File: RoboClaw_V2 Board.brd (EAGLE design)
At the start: 49 x 23.6 mm, 7 parts

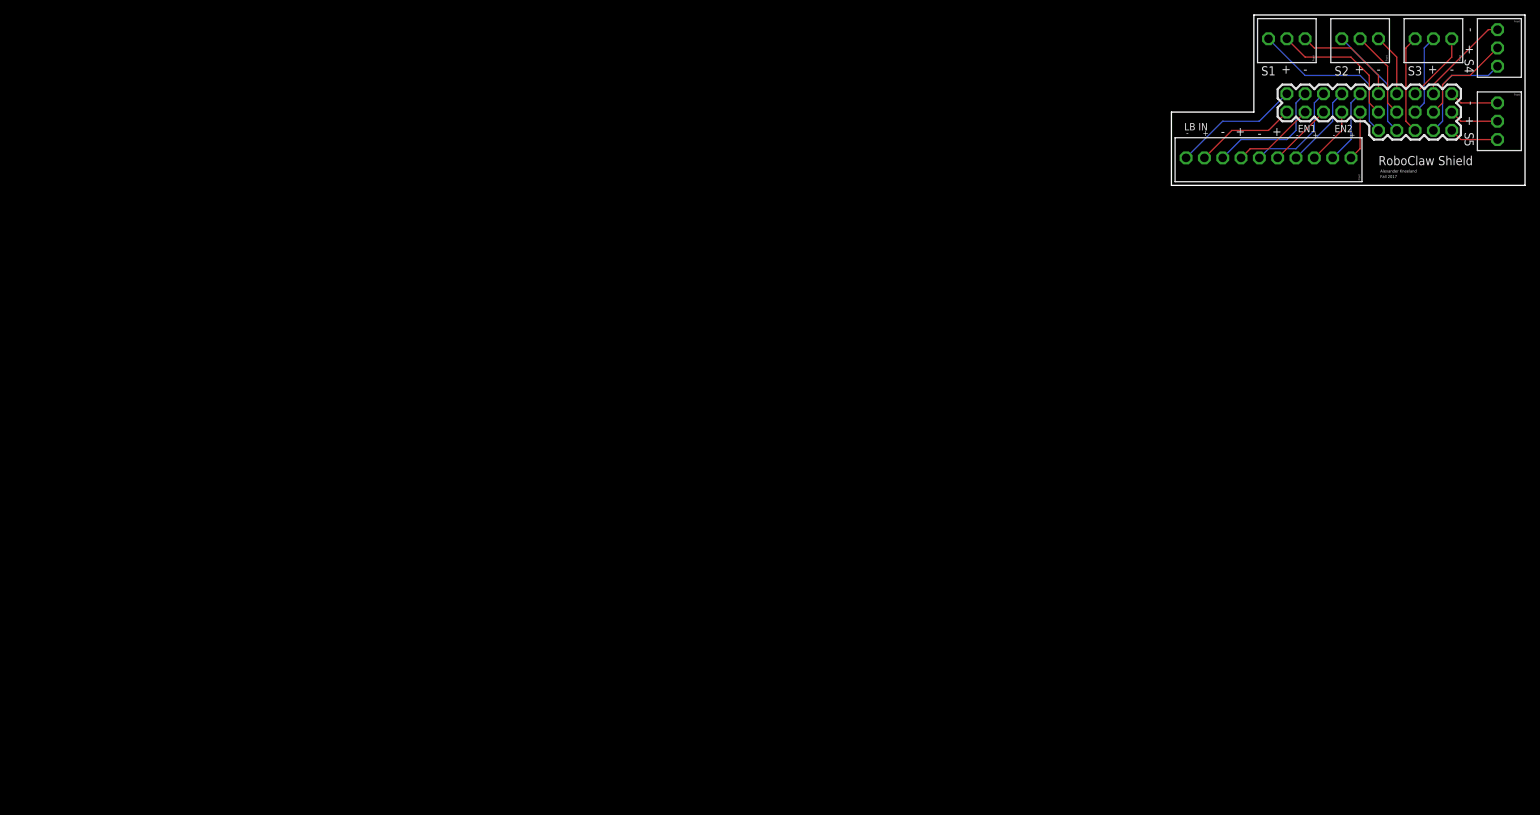
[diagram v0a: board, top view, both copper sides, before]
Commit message: Added in some new connectors in the schematic and resized board
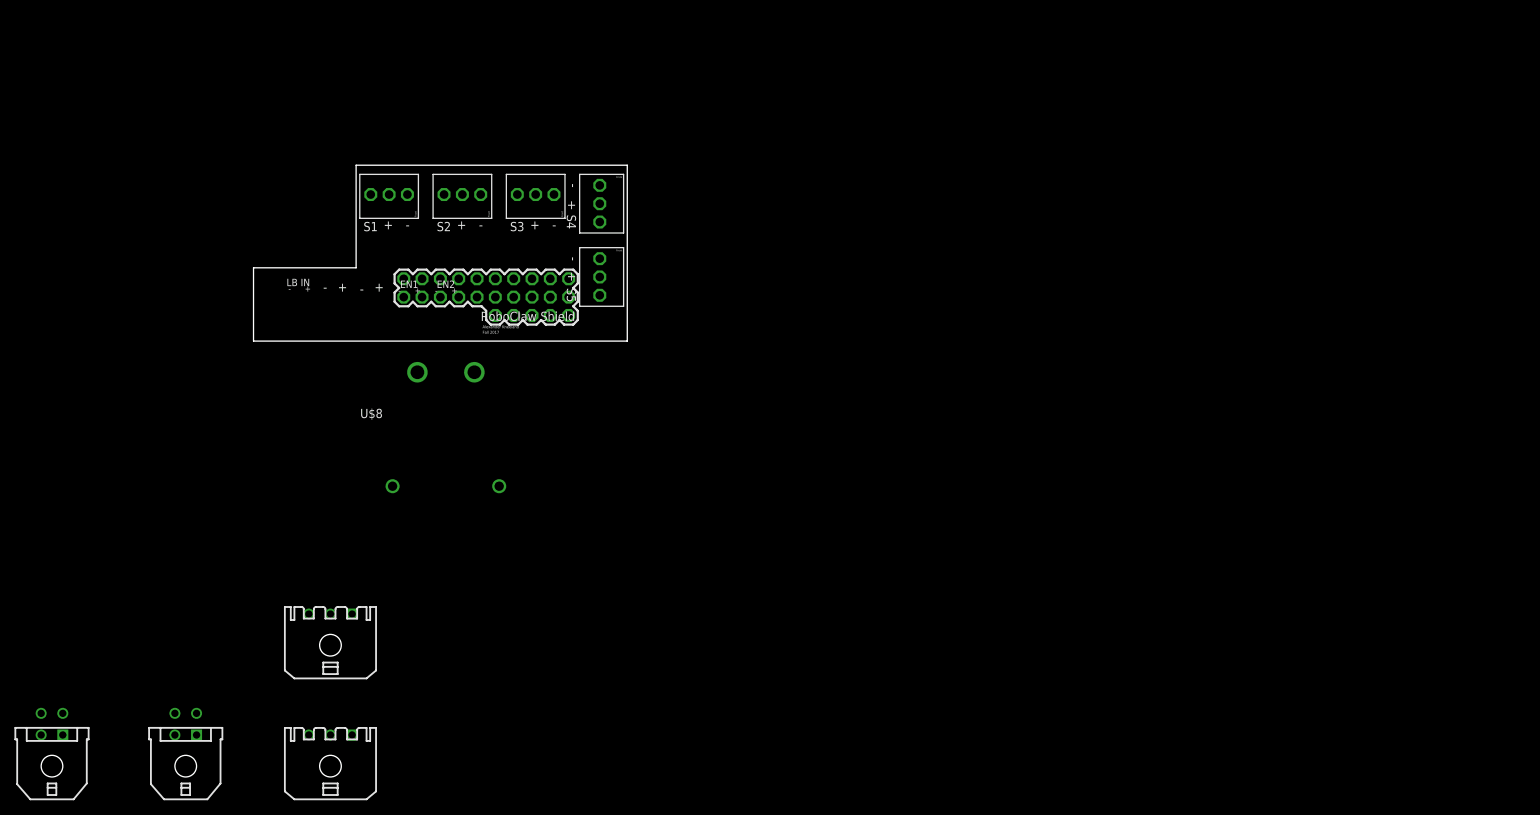
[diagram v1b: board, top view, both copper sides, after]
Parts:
- removed U$2: 10_PIN, Screw Blocks:10_PIN
- added U$8: (no value), 000_CustomPartsMaster:ANDERSON_RIGHTANGLE_X2
- added X1, X2: (no value), con-molex-micro-fit-3_0:43650-0300
- added X3, X4: (no value), con-molex-micro-fit-3_0:43045-0400
- moved U$5 126.3 mm to (-21.6, 21.6)
- moved U$3 126.3 mm to (-5.08, 0.00)
- moved U$4 126.3 mm to (-5.08, 10.2)
- moved U$6 126.3 mm to (-31.8, 21.6)
- moved U$7 126.3 mm to (-41.9, 21.6)
- moved U$1 125.1 mm to (-20.8, 3.56)
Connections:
- removed net N$10: U$1.P$12, U$6.P$1
- removed net N$13: U$1.P$15, U$7.P$1
- removed net N$14: U$1.P$14, U$7.P$2
- removed net N$16: U$1.P$18, U$2.P$3
- removed net N$17: U$1.P$21, U$2.P$6
- removed net N$18: U$1.P$20, U$2.P$5
- removed net N$19: U$1.P$23, U$2.P$8
- removed net N$20: U$1.P$22, U$2.P$7
- removed net N$21: U$1.P$24, U$2.P$9
- removed net N$22: U$1.P$25, U$2.P$10
- removed net N$24: U$1.P$17, U$2.P$2
- removed net N$25: U$1.P$16, U$2.P$1
- removed net N$26: U$1.P$19, U$2.P$4
- removed net N$28: U$1.P$13, U$7.P$3
- removed net N$4: U$1.P$6, U$4.P$1
- removed net N$5: U$1.P$5, U$4.P$2
- new net EN1_+: U$1.P$20
- new net EN1_A: U$1.P$18
- new net EN2_+: U$1.P$22
- new net EN2_A: U$1.P$16
- new net LB_+: U$1.P$24
- new net N$29: U$1.P$12
- new net N$30: U$1.P$11
- new net N$31: U$1.P$10
- new net N$32: U$1.P$15
- new net N$33: U$1.P$14
- net N$1: now also U$1.P$17; no longer U$1.P$1, U$3.P$3
- net N$11: now also U$1.P$5; no longer U$1.P$11, U$6.P$2
- net N$12: now also U$1.P$4; no longer U$1.P$10, U$6.P$3
- net N$2: now also U$1.P$19; no longer U$1.P$2, U$3.P$2
- net N$3: now also U$1.P$21; no longer U$1.P$3, U$3.P$1
- net N$6: no longer U$1.P$4
- net N$7: no longer U$5.P$1
- net N$8: no longer U$5.P$2
- net N$9: no longer U$5.P$3
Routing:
- net N$28: track 23.5 -> 0.00 mm
- net N$14: track 19.1 -> 0.00 mm
- net N$22: track 17.7 -> 0.00 mm
- net N$19: track 17.3 -> 0.00 mm
- net N$12: track 15.9 -> 0.00 mm
- net N$6: track 15.5 -> 0.00 mm
- net N$17: track 14.8 -> 0.00 mm
- net N$13: track 14.8 -> 0.00 mm
- net N$5: track 14.1 -> 0.00 mm
- net N$21: track 14.1 -> 0.00 mm
- net N$9: track 13.8 -> 0.00 mm
- net N$4: track 13.3 -> 0.00 mm
- net N$11: track 12.3 -> 0.00 mm
- net N$26: track 11.5 -> 0.00 mm
- net N$20: track 11.5 -> 0.00 mm
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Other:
- board size 49 x 23.6 mm -> 51.8 x 24.4 mm

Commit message: connected nets to encoders/serial lines/battery
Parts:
- removed U$3, U$4, U$5, U$6, U$7: (no value), Screw Blocks:3_PIN
- renumbered X1 to SERIAL_IN, X2 to SERIAL_OUT, X3 to ENC2, X4 to ENC1
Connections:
- removed net N$1: U$1.P$17
- removed net N$11: U$1.P$5
- removed net N$12: U$1.P$4
- removed net N$2: U$1.P$19
- removed net N$29: U$1.P$12
- removed net N$3: U$1.P$21
- removed net N$30: U$1.P$11
- removed net N$31: U$1.P$10
- removed net N$32: U$1.P$15
- removed net N$6: U$4.P$3
- removed net N$7: U$1.P$9
- removed net N$8: U$1.P$8
- new net ENC1_+: ENC1.P$4
- new net ENC1_-: ENC1.P$3, U$1.P$21
- new net ENC1_A: ENC1.P$2
- new net ENC1_B: ENC1.P$1, U$1.P$17
- new net ENC2_+: ENC2.P$4
- new net ENC2_-: ENC2.P$3, U$1.P$23
- new net ENC2_A: ENC2.P$2
- new net ENC2_B: ENC2.P$1, U$1.P$19
- new net GND: SERIAL_IN.P$1, SERIAL_OUT.P$3, U$1.P$12, U$1.P$15, U$1.P$3, U$1.P$6, U$1.P$9
- new net LB+: U$8.P1
- new net LB-: U$1.P$25, U$8.P2
- new net S1/RX: SERIAL_OUT.P$2
- new net S1/TX: SERIAL_IN.P$3, SERIAL_OUT.P$1, U$1.P$13
- new net S2/RX: SERIAL_IN.P$2, U$1.P$10
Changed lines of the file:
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@@
 <drawing>
 <settings>
-<setting alwaysvectorfont="no"/>
+<setting alwaysvectorfont="yes"/>
 <setting verticaltext="up"/>
 </settings>
@@
 <elements>
 <element name="U$1" library="Screw Blocks" package="ROBOCLAW_PINS" value="ROBOCLAW_PINS" x="-20.828" y="3.556"/>
-<element name="U$3" library="Screw Blocks" package="3_PIN" value="" x="-5.08" y="0"/>
-<element name="U$4" library="Screw Blocks" package="3_PIN" value="" x="-5.08" y="10.16"/>
-<element name="U$5" library="Screw Blocks" package="3_PIN" value="" x="-21.59" y="21.59" rot="R270"/>
-<element name="U$6" library="Screw Blocks" package="3_PIN" value="" x="-31.75" y="21.59" rot="R270"/>
-<element name="U$7" library="Screw Blocks" package="3_PIN" value="" x="-41.91" y="21.59" rot="R270"/>
 <element name="U$8" library="000_CustomPartsMaster" package="ANDERSON_RIGHTANGLE_X2" value="" x="-25.146" y="-4.318" rot="R180"/>
-<element name="X1" library="con-molex-micro-fit-3_0" package="43650-0300" value="" x="-41.148" y="-42.164"/>
-<element name="X2" library="con-molex-micro-fit-3_0" package="43650-0300" value="" x="-41.148" y="-58.928"/>
-<element name="X3" library="con-molex-micro-fit-3_0" package="43045-0400" value="" x="-61.214" y="-58.928">
+<element name="SERIAL_IN" library="con-molex-micro-fit-3_0" package="43650-0300" value="" x="-41.148" y="-42.164"/>
+<element name="SERIAL_OUT" library="con-molex-micro-fit-3_0" package="43650-0300" value="" x="-41.148" y="-58.928"/>
+<element name="ENC2" library="con-molex-micro-fit-3_0" package="43045-0400" value="" x="-61.214" y="-58.928">
 <attribute name="MATERIAL" value="" x="-61.214" y="-58.928" size="1.778" layer="27" display="off"/>
 </element>
-<element name="X4" library="con-molex-micro-fit-3_0" package="43045-0400" value="" x="-79.756" y="-58.928">
+<element name="ENC1" library="con-molex-micro-fit-3_0" package="43045-0400" value="" x="-79.756" y="-58.928">
 <attribute name="MATERIAL" value="" x="-79.756" y="-58.928" size="1.778" layer="27" display="off"/>
 </element>
 </elements>
 <signals>
-<signal name="N$6">
-<contactref element="U$4" pad="P$3"/>
-</signal>
-<signal name="N$7">
-<contactref element="U$1" pad="P$9"/>
-</signal>
-<signal name="N$8">
-<contactref element="U$1" pad="P$8"/>
-</signal>
 <signal name="N$9">
 <contactref element="U$1" pad="P$7"/>
@@
 <contactref element="U$1" pad="P$24"/>
 </signal>
-<signal name="N$29">
-<contactref element="U$1" pad="P$12"/>
-</signal>
-<signal name="N$30">
-<contactref element="U$1" pad="P$11"/>
-</signal>
-<signal name="N$31">
+<signal name="S2/RX">
 <contactref element="U$1" pad="P$10"/>
-</signal>
-<signal name="N$32">
-<contactref element="U$1" pad="P$15"/>
+<contactref element="SERIAL_IN" pad="P$2"/>
+<wire x1="-15.748" y1="3.556" x2="-41.148" y2="-37.844" width="0" layer="19" extent="1-1"/>
+</signal>
+<signal name="ENC1_B">
+<contactref element="U$1" pad="P$17"/>
+<contactref element="ENC1" pad="P$1"/>
+<wire x1="-20.828" y1="8.636" x2="-78.256" y2="-54.608" width="0" layer="19" extent="1-1"/>
 </signal>
 <signal name="N$33">
 <contactref element="U$1" pad="P$14"/>
 </signal>
-<signal name="N$11">
-<contactref element="U$1" pad="P$5"/>
-</signal>
-<signal name="N$12">
-<contactref element="U$1" pad="P$4"/>
-</signal>
-<signal name="N$1">
-<contactref element="U$1" pad="P$17"/>
-</signal>
-<signal name="N$2">
+<signal name="ENC2_B">
 <contactref element="U$1" pad="P$19"/>
-</signal>
-<signal name="N$3">
+<contactref element="ENC2" pad="P$1"/>
+<wire x1="-23.368" y1="8.636" x2="-59.714" y2="-54.608" width="0" layer="19" extent="1-1"/>
+</signal>
+<signal name="ENC1_-">
 <contactref element="U$1" pad="P$21"/>
+<contactref element="ENC1" pad="P$3"/>
+<wire x1="-25.908" y1="8.636" x2="-78.256" y2="-51.608" width="0" layer="19" extent="1-1"/>
+</signal>
+<signal name="LB-">
+<contactref element="U$1" pad="P$25"/>
+<contactref element="U$8" pad="P2"/>
+<wire x1="-30.988" y1="8.636" x2="-29.096" y2="-4.318" width="0" layer="19" extent="1-1"/>
+</signal>
+<signal name="ENC2_-">
+<contactref element="U$1" pad="P$23"/>
+<contactref element="ENC2" pad="P$3"/>
+<wire x1="-28.448" y1="8.636" x2="-59.714" y2="-51.608" width="0" layer="19" extent="1-1"/>
+</signal>
+<signal name="GND">
+<contactref element="U$1" pad="P$3"/>
+<contactref element="U$1" pad="P$6"/>
+<contactref element="U$1" pad="P$9"/>
+<contactref element="U$1" pad="P$12"/>
+<contactref element="U$1" pad="P$15"/>
+<contactref element="SERIAL_OUT" pad="P$3"/>
+<contactref element="SERIAL_IN" pad="P$1"/>
+<wire x1="-38.148" y1="-37.844" x2="-44.148" y2="-54.608" width="0" layer="19" extent="1-1"/>
+<wire x1="-18.288" y1="8.636" x2="-38.148" y2="-37.844" width="0" layer="19" extent="1-1"/>
+<wire x1="-15.748" y1="8.636" x2="-18.288" y2="8.636" width="0" layer="19" extent="1-1"/>
+<wire x1="-13.208" y1="8.636" x2="-15.748" y2="8.636" width="0" layer="19" extent="1-1"/>
+<wire x1="-10.668" y1="8.636" x2="-13.208" y2="8.636" width="0" layer="19" extent="1-1"/>
+<wire x1="-8.128" y1="8.636" x2="-10.668" y2="8.636" width="0" layer="19" extent="1-1"/>
+</signal>
+<signal name="S1/TX">
+<contactref element="U$1" pad="P$13"/>
+<contactref element="SERIAL_IN" pad="P$3"/>
+<contactref element="SERIAL_OUT" pad="P$1"/>
+<wire x1="-44.148" y1="-37.844" x2="-38.148" y2="-54.608" width="0" layer="19" extent="1-1"/>
+<wire x1="-18.288" y1="3.556" x2="-44.148" y2="-37.844" width="0" layer="19" extent="1-1"/>
+</signal>
+<signal name="ENC1_+">
+<contactref element="ENC1" pad="P$4"/>
+</signal>
+<signal name="ENC1_A">
+<contactref element="ENC1" pad="P$2"/>
+</signal>
+<signal name="ENC2_+">
+<contactref element="ENC2" pad="P$4"/>
+</signal>
+<signal name="ENC2_A">
+<contactref element="ENC2" pad="P$2"/>
+</signal>
+<signal name="S1/RX">
+<contactref element="SERIAL_OUT" pad="P$2"/>
+</signal>
+<signal name="LB+">
+<contactref element="U$8" pad="P1"/>
 </signal>
 </signals>
